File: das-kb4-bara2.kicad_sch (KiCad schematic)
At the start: 0 parts

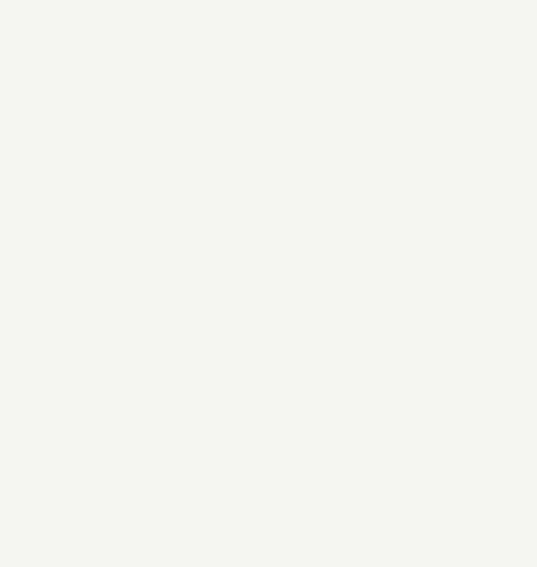
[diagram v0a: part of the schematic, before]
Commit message: sch nearing completion.
usb side done.
needs mcu power supply sorting out.
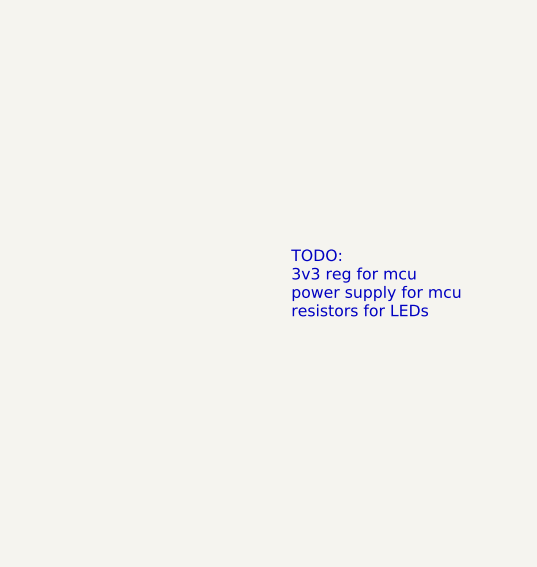
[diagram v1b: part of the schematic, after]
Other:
- note added: "TODO: 3v3 reg for mcu power supply for mcu resistors for LEDs"
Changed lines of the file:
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@@
 (kicad_sch (version 20230121) (generator eeschema)
   (paper "A4")
+  (text "TODO:\n3v3 reg for mcu\npower supply for mcu\nresistors for LEDs"
+    (at 185.42 93.98 0)
+    (effects (font (size 1.27 1.27)) (justify left bottom))
+  )
   (sheet (at 101.6 101.6) (size 50.8 25.4) (fields_autoplaced)
     (stroke (width 0.1524) (type solid))

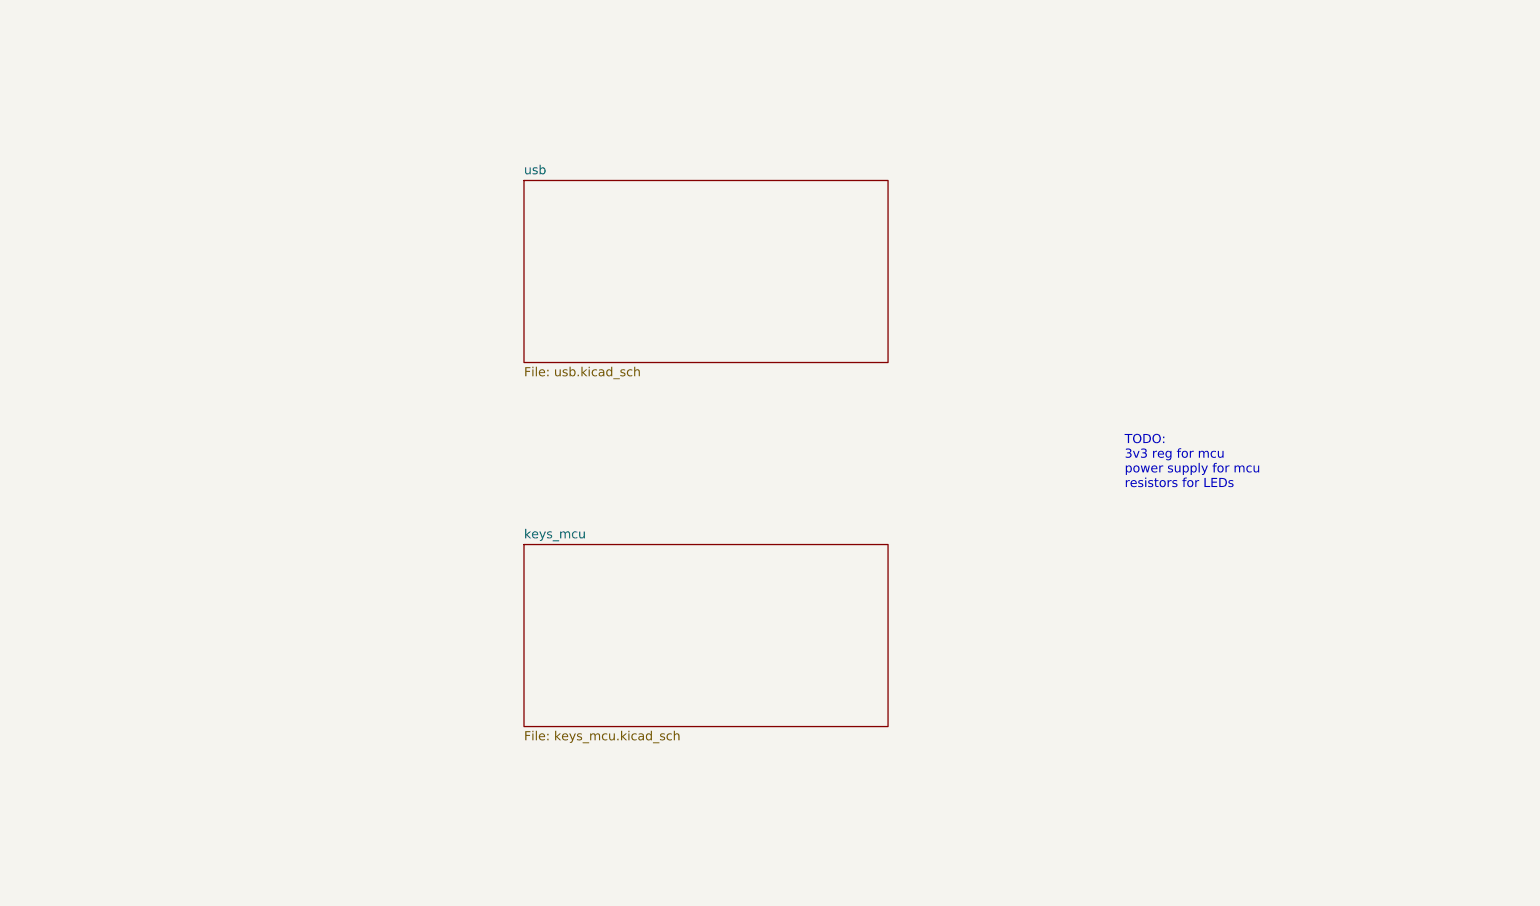
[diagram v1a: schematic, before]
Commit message: schematic "done" footprints all assigned
Need working calipers to start getting the board outline and fixed
positions, but ... mostly there?

schematic needs "polish" now, more introductions, cleaner text layouts,
probably more optional test points, throw more caps at it.
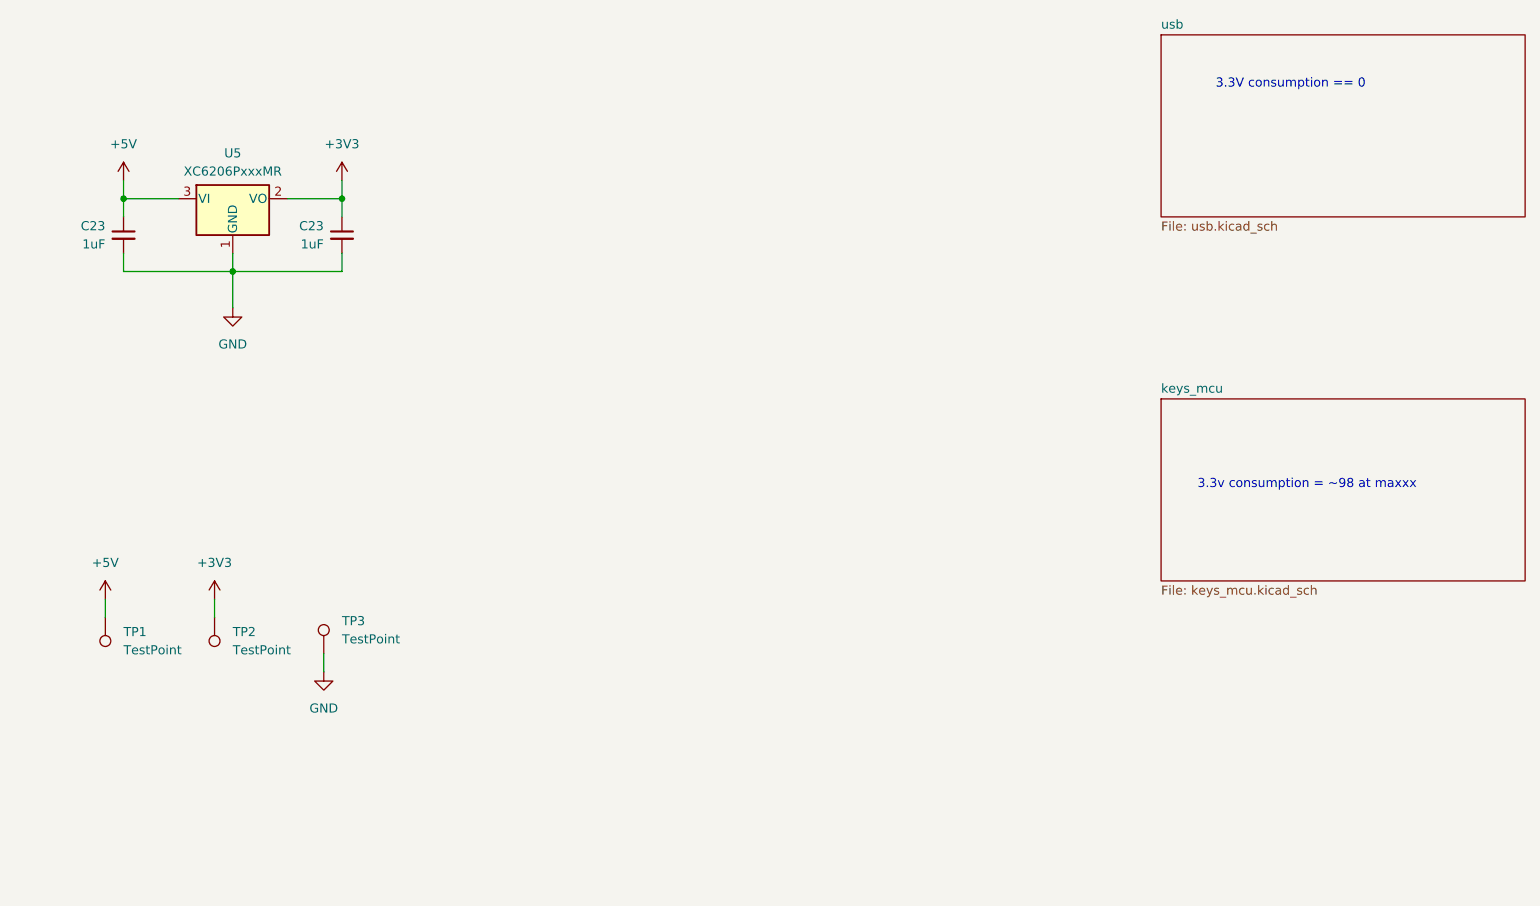
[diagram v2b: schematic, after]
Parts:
- added C23 (x2): 1uF, Capacitor_SMD:C_0603_1608Metric, symbol Device:C_Small
- added TP1, TP2, TP3: TestPoint, TestPoint:TestPoint_THTPad_D1.5mm_Drill0.7mm, symbol Connector:TestPoint
- added U5: XC6206PxxxMR, Package_TO_SOT_SMD:SOT-23-3, symbol Regulator_Linear:XC6206PxxxMR
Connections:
- new net +3V3: C23.1, TP2.1, U5.2 (VO)
- new net +5V: C23.1, TP1.1, U5.3 (VI)
- new net GND: C23.2, C23.2, TP3.1, U5.1 (GND)
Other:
- note added: "3.3V consumption == 0"
- note added: "3.3v consumption = ~98 at maxxx"
- note removed: "TODO: 3v3 reg for mcu power supply for mcu resistors for LEDs"

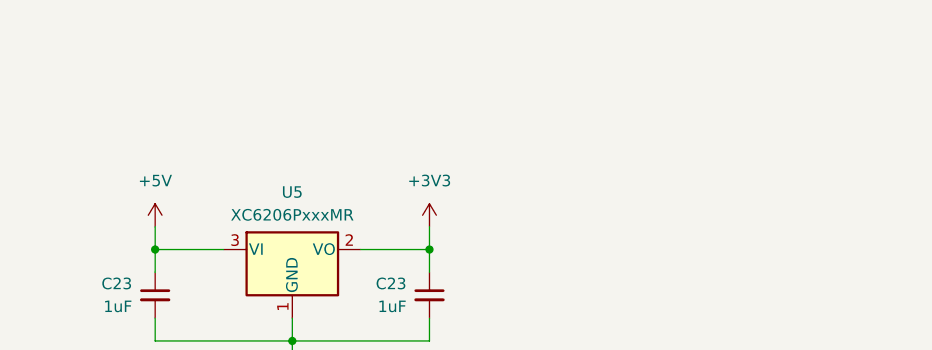
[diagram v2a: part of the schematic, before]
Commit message: add "bonus" can transceiver ;)
this is so we can use the round 1 protos for another project...

also: replace srv05 with an alternate, also jlc preferred, but cheaper
part.  Update power budgets.

We've done some initial work with the pcb, but we're running into weird
kicad wx bugs, so we're going to save it all here, and commit, and
perhaps continue with 7.99.....
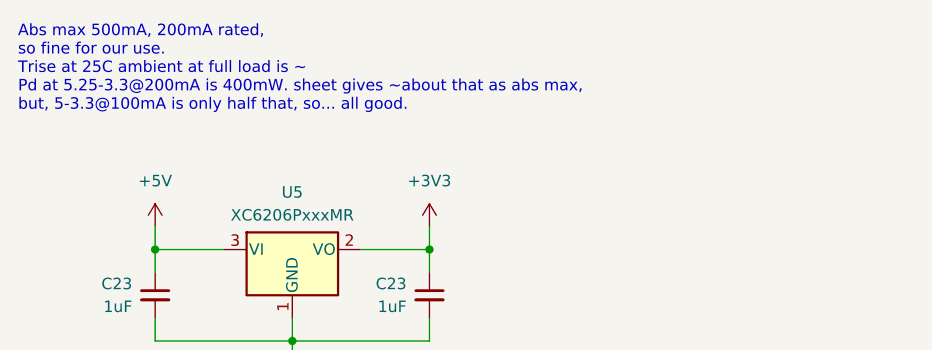
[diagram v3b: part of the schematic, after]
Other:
- note added: "Abs max 500mA, 200mA rated, so fine for our use. Trise at 25C ambient at full load is ~ Pd at 5.25-3.3@200mA is 400mW. sheet gives ~about that as abs max, but, 5-3.3@100mA is only half that, so... all good."
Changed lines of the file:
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@@
     (stroke (width 0) (type default))
+  )
+  (text "Abs max 500mA, 200mA rated,\nso fine for our use.\nTrise at 25C ambient at full load is ~\nPd at 5.25-3.3@200mA is 400mW. sheet gives ~about that as abs max,\nbut, 5-3.3@100mA is only half that, so... all good."
+    (at 30.48 38.1 0)
+    (effects (font (size 1.27 1.27)) (justify left bottom))
   )
   (text "3.3V consumption == 0" (at 198.12 38.1 0)
@@
       (effects (font (size 1.27 1.27)) hide)
     )
+    (property "lcsc2#" "" (at 58.42 111.76 0)
+      (effects (font (size 1.27 1.27)) hide)
+    )
     (pin "1")
     (instances
@@
     )
     (property "Datasheet" "~" (at 38.1 111.76 0)
+      (effects (font (size 1.27 1.27)) hide)
+    )
+    (property "lcsc2#" "" (at 43.18 111.76 0)
       (effects (font (size 1.27 1.27)) hide)
     )
@@
       (effects (font (size 1.27 1.27)) hide)
     )
+    (property "lcsc2#" "" (at 60.96 53.34 0)
+      (effects (font (size 1.27 1.27)) hide)
+    )
     (pin "1")
     (pin "3")
@@
     )
     (property "lcsc#" "C15849" (at 76.2 58.42 0)
+      (effects (font (size 1.27 1.27)) hide)
+    )
+    (property "lcsc2#" "" (at 76.2 58.42 0)
       (effects (font (size 1.27 1.27)) hide)
     )
@@
       (effects (font (size 1.27 1.27)) hide)
     )
+    (property "lcsc2#" "" (at 45.72 58.42 0)
+      (effects (font (size 1.27 1.27)) hide)
+    )
     (pin "1")
     (pin "2")
@@
       (effects (font (size 1.27 1.27)) hide)
     )
+    (property "lcsc2#" "" (at 73.66 116.84 0)
+      (effects (font (size 1.27 1.27)) hide)
+    )

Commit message: routing progress
Just nice to make some save points every now and again.
USB seems... ok?  Still need to check 3v3 or 5v on the power pullups,
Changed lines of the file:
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@@
+    (stroke (width 0) (type default))
+  )
+  (wire (pts (xy 76.2 53.34) (xy 81.28 53.34))
     (stroke (width 0) (type default))
   )
@@
     (effects (font (size 1.27 1.27)) (justify left bottom))
   )
+  (netclass_flag "" (length 2.54) (shape round) (at 81.28 53.34 0) (fields_autoplaced)
+    (effects (font (size 1.27 1.27)) (justify left bottom))
+    (property "Netclass" "Power distribution" (at 81.9785 50.8 0)
+      (effects (font (size 1.27 1.27) italic) (justify left))
+    )
+  )
   (symbol (lib_id "power:+5V") (at 43.18 109.22 0) (unit 1)

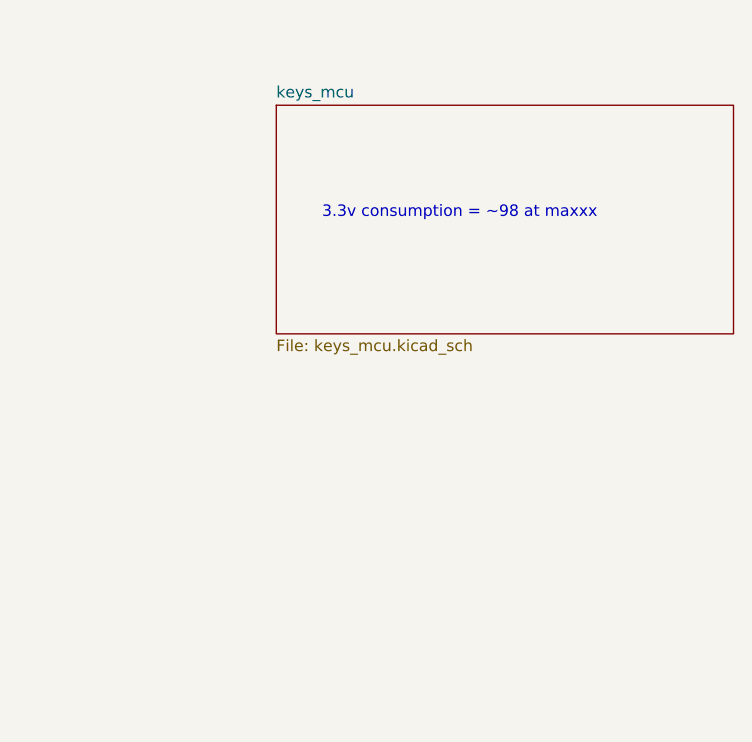
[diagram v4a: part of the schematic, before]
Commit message: cleanup schematic, break out most of it
Broke it all out to the right places, now I can go and shuffle all the
labels to make it line up.  Thankfully we can just "freely" route the
keybaord matrix pins!
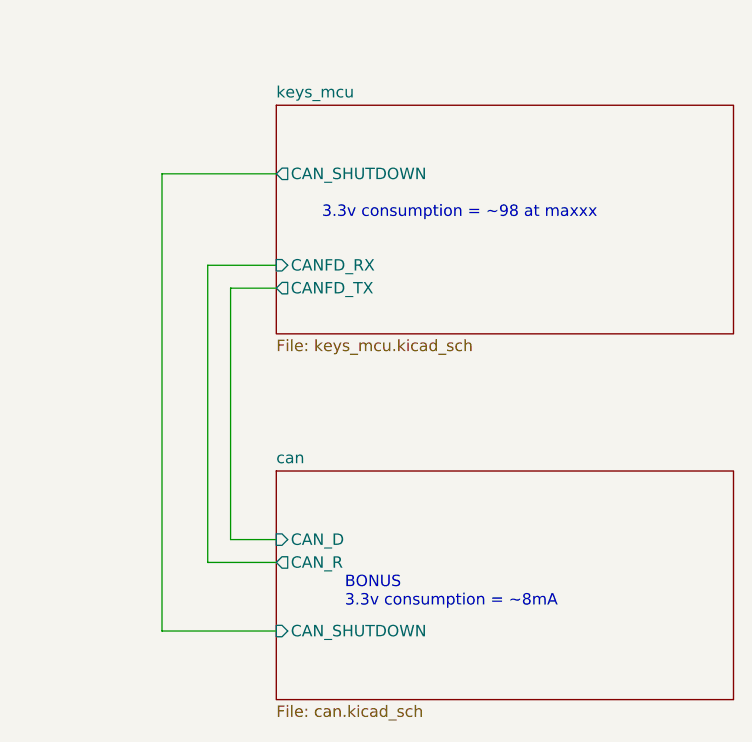
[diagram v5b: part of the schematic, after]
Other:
- added sheet can (can.kicad_sch)
- sheet keys_mcu ports: added CANFD_RX, CANFD_TX, CAN_SHUTDOWN; removed none
- note added: "BONUS 3.3v consumption = ~8mA"
- company: (none) -> Ekta Labs
- title: (none) -> Das KB4-Bara2
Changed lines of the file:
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@@
 (kicad_sch (version 20230121) (generator eeschema)
   (paper "A4")
+  (title_block
+    (title "Das KB4-Bara2")
+    (company "Ekta Labs")
+    (comment 1 "http://github.com/karlp/das-kb4-bara2")
+  )
   (junction (at 60.96 63.5) (diameter 0) (color 0 0 0 0)
   )
@@
     (stroke (width 0) (type default))
   )
+  (wire (pts (xy 190.5 132.08) (xy 182.88 132.08))
+    (stroke (width 0) (type default))
+  )
   (wire (pts (xy 76.2 53.34) (xy 81.28 53.34))
     (stroke (width 0) (type default))
   )
+  (wire (pts (xy 185.42 101.6) (xy 185.42 129.54))
+    (stroke (width 0) (type default))
+  )
   (wire (pts (xy 76.2 53.34) (xy 76.2 55.88))
     (stroke (width 0) (type default))
@@
     (stroke (width 0) (type default))
   )
+  (wire (pts (xy 177.8 139.7) (xy 190.5 139.7))
+    (stroke (width 0) (type default))
+  )
   (wire (pts (xy 45.72 53.34) (xy 45.72 55.88))
     (stroke (width 0) (type default))
@@
     (stroke (width 0) (type default))
   )
+  (wire (pts (xy 182.88 132.08) (xy 182.88 99.06))
+    (stroke (width 0) (type default))
+  )
   (wire (pts (xy 76.2 50.8) (xy 76.2 53.34))
     (stroke (width 0) (type default))
@@
     (stroke (width 0) (type default))
   )
+  (wire (pts (xy 185.42 129.54) (xy 190.5 129.54))
+    (stroke (width 0) (type default))
+  )
   (wire (pts (xy 45.72 50.8) (xy 45.72 53.34))
     (stroke (width 0) (type default))
   )
+  (wire (pts (xy 177.8 88.9) (xy 177.8 139.7))
+    (stroke (width 0) (type default))
+  )
   (wire (pts (xy 68.58 53.34) (xy 76.2 53.34))
     (stroke (width 0) (type default))
@@
     (stroke (width 0) (type default))
   )
+  (wire (pts (xy 182.88 99.06) (xy 190.5 99.06))
+    (stroke (width 0) (type default))
+  )
   (wire (pts (xy 60.96 63.5) (xy 60.96 68.58))
     (stroke (width 0) (type default))
@@
     (stroke (width 0) (type default))
   )
+  (wire (pts (xy 190.5 88.9) (xy 177.8 88.9))
+    (stroke (width 0) (type default))
+  )
   (wire (pts (xy 73.66 116.84) (xy 73.66 119.38))
+    (stroke (width 0) (type default))
+  )
+  (wire (pts (xy 190.5 101.6) (xy 185.42 101.6))
     (stroke (width 0) (type default))
   )
@@
   )
   (text "3.3V consumption == 0" (at 198.12 38.1 0)
+    (effects (font (size 1.27 1.27)) (justify left bottom))
+  )
+  (text "BONUS\n3.3v consumption = ~8mA" (at 198.12 137.16 0)
     (effects (font (size 1.27 1.27)) (justify left bottom))
   )
@@
       (effects (font (size 1.27 1.27)) (justify left top))
     )
+    (pin "CANFD_RX" input (at 190.5 99.06 180)
+      (effects (font (size 1.27 1.27)) (justify left))
+    )
+    (pin "CANFD_TX" output (at 190.5 101.6 180)
+      (effects (font (size 1.27 1.27)) (justify left))
+    )
+    (pin "CAN_SHUTDOWN" output (at 190.5 88.9 180)
+      (effects (font (size 1.27 1.27)) (justify left))
+    )
     (instances
       (project "das-kb4-bara2"
@@
       )
     )
+  )
+  (sheet (at 190.5 121.92) (size 50.8 25.4) (fields_autoplaced)
+    (stroke (width 0.1524) (type solid))
+    (fill (color 0 0 0 0.0000))
+    (property "Sheetname" "can" (at 190.5 121.2084 0)
+      (effects (font (size 1.27 1.27)) (justify left bottom))
+    )
+    (property "Sheetfile" "can.kicad_sch" (at 190.5 147.9046 0)
+      (effects (font (size 1.27 1.27)) (justify left top))
+    )
+    (pin "CAN_D" input (at 190.5 129.54 180)
+      (effects (font (size 1.27 1.27)) (justify left))
+    )
+    (pin "CAN_R" output (at 190.5 132.08 180)
+      (effects (font (size 1.27 1.27)) (justify left))
+    )
+    (pin "CAN_SHUTDOWN" input (at 190.5 139.7 180)
+      (effects (font (size 1.27 1.27)) (justify left))
+    )
+    (instances
+      (project "das-kb4-bara2"
+        (path "/d0e4eaec-96cb-4a0e-a384-5b3e3f5f8d5d" (page "4"))
+      )
+    )

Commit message: shuffled, added bonus, silked up...
Nearly there..?
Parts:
- TP1: value TestPoint -> 5V
- TP2: value TestPoint -> 3v3
- TP3: value TestPoint -> GND
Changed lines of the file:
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@@
       (effects (font (size 1.27 1.27)) (justify right))
     )
-    (property "Value" "TestPoint" (at 60.96 116.332 0)
+    (property "Value" "3v3" (at 60.96 116.332 0)
       (effects (font (size 1.27 1.27)) (justify right))
     )
@@
       (effects (font (size 1.27 1.27)) (justify right))
     )
-    (property "Value" "TestPoint" (at 45.72 116.332 0)
+    (property "Value" "5V" (at 45.72 116.332 0)
       (effects (font (size 1.27 1.27)) (justify right))
     )
@@
       (effects (font (size 1.27 1.27)) (justify left))
     )
-    (property "Value" "TestPoint" (at 76.2 114.808 0)
+    (property "Value" "GND" (at 76.2 114.808 0)
       (effects (font (size 1.27 1.27)) (justify left))
     )
